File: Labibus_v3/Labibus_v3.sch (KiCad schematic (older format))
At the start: 33 parts

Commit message: update started on first pcb layout
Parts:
- added J13, J14, J15, J16, J4, J5, J6, J7: Conn_01x03, Connector_PinSocket_2.54mm:PinSocket_1x03_P2.54mm_Vertical, symbol Connector_Generic:Conn_01x03
- C1, C2, C3, C4, C5, C6, C7: renamed from C?; footprint (none) -> Capacitor_SMD:C_0603_1608Metric_Pad1.08x0.95mm_HandSolder
- D1, D2, D3: renamed from D?; footprint (none) -> LED_SMD:LED_0603_1608Metric_Pad1.05x0.95mm_HandSolder
- J1: renamed from J?; footprint (none) -> TerminalBlock_Phoenix:TerminalBlock_Phoenix_MPT-0,5-4-2.54_1x04_P2.54mm_Horizontal
- J10, J11, J12, J2, J3, J8, J9: renamed from J?; footprint (none) -> Connector_PinSocket_2.54mm:PinSocket_1x03_P2.54mm_Vertical
- R1, R2, R3, R4, R5, R6, R7, R8, R9: renamed from R?; footprint (none) -> Resistor_SMD:R_0603_1608Metric_Pad0.98x0.95mm_HandSolder
- RN1: renamed from RN?; footprint (none) -> Resistor_SMD:R_Array_Concave_4x0603
- SW1: renamed from SW?; footprint (none) -> Button_Switch_SMD:SW_SPST_EVQPE1
- U2: renamed from U?; footprint (none) -> Package_SO:SOIC-8_3.9x4.9mm_P1.27mm
- Y1: renamed from Y?; footprint (none) -> Crystal:Resonator_SMD_muRata_CSTxExxV-3Pin_3.0x1.1mm_HandSoldering
- gave numbers to parts that had none: 2
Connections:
- net D6 is gone; now on net ARDUINO_P6: U3.10 (PD6)
- net D7 is gone; now on net ARDUINO_P7: U3.11 (PD7)
- net RX is gone; now on net ARDUINO_P_RX: J3.4 (Pin_4)
- net TX is gone; now on net ARDUINO_P_TX: J3.5 (Pin_5)
- net +5V: now also J13.2 (Pin_2), J14.2 (Pin_2), J15.2 (Pin_2), J16.2 (Pin_2), J4.2 (Pin_2), J5.2 (Pin_2), J6.2 (Pin_2), J7.2 (Pin_2)
- net A6: now also J6.3 (Pin_3)
- net A7: now also J15.3 (Pin_3)
- net D2: now also J4.3 (Pin_3)
- net D3: now also J13.3 (Pin_3)
- net D4: now also J5.3 (Pin_3)
- net D5: now also J14.3 (Pin_3)
- net D8: now also J7.3 (Pin_3)
- net D9: now also J16.3 (Pin_3)
- net GND: now also J13.1 (Pin_1), J14.1 (Pin_1), J15.1 (Pin_1), J16.1 (Pin_1), J4.1 (Pin_1), J5.1 (Pin_1), J6.1 (Pin_1), J7.1 (Pin_1)
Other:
- note added: "A6-pinout"
- note added: "A7-pinout"
- note added: "D2-pinout"
- note added: "D3-pinout"
- note added: "D4-pinout"
- note added: "D5-pinout"
- note added: "D8-pinout"
- note added: "D9-pinout"
- moved on the sheet: C6, C7, U3

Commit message: new update to the pcb layout Note: Change pin row to 13 on the left side to shrink the size
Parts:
- J10: footprint Connector_PinSocket_2.54mm:PinSocket_1x03_P2.54mm_Vertical -> Connector_PinSocket_2.54mm:PinSocket_1x06_P2.54mm_Vertical
- J2: footprint Connector_PinSocket_2.54mm:PinSocket_1x03_P2.54mm_Vertical -> Connector_PinHeader_2.54mm:PinHeader_1x04_P2.54mm_Vertical
- J3: footprint Connector_PinSocket_2.54mm:PinSocket_1x03_P2.54mm_Vertical -> Connector_PinHeader_2.54mm:PinHeader_1x06_P2.54mm_Vertical
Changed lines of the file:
@@
 F 0 "J3" H 8093 1442 50  0000 C CNN
 F 1 "Conn_01x06" H 8093 1351 50  0000 C CNN
-F 2 "Connector_PinSocket_2.54mm:PinSocket_1x03_P2.54mm_Vertical" H 8175 1025 50  0001 C CNN
+F 2 "Connector_PinHeader_2.54mm:PinHeader_1x06_P2.54mm_Vertical" H 8175 1025 50  0001 C CNN
 F 3 "~" H 8175 1025 50  0001 C CNN
 	1    8175 1025
@@
 F 0 "J10" H 10605 1042 50  0000 L CNN
 F 1 "Conn_01x06" H 10605 951 50  0000 L CNN
-F 2 "Connector_PinSocket_2.54mm:PinSocket_1x03_P2.54mm_Vertical" H 10525 1050 50  0001 C CNN
+F 2 "Connector_PinSocket_2.54mm:PinSocket_1x06_P2.54mm_Vertical" H 10525 1050 50  0001 C CNN
 F 3 "~" H 10525 1050 50  0001 C CNN
 	1    10525 1050
@@
 F 0 "J2" H 8055 1792 50  0000 L CNN
 F 1 "Conn_01x04" H 8055 1701 50  0000 L CNN
-F 2 "Connector_PinSocket_2.54mm:PinSocket_1x03_P2.54mm_Vertical" H 7975 1800 50  0001 C CNN
+F 2 "Connector_PinHeader_2.54mm:PinHeader_1x04_P2.54mm_Vertical" H 7975 1800 50  0001 C CNN
 F 3 "~" H 7975 1800 50  0001 C CNN
 	1    7975 1800

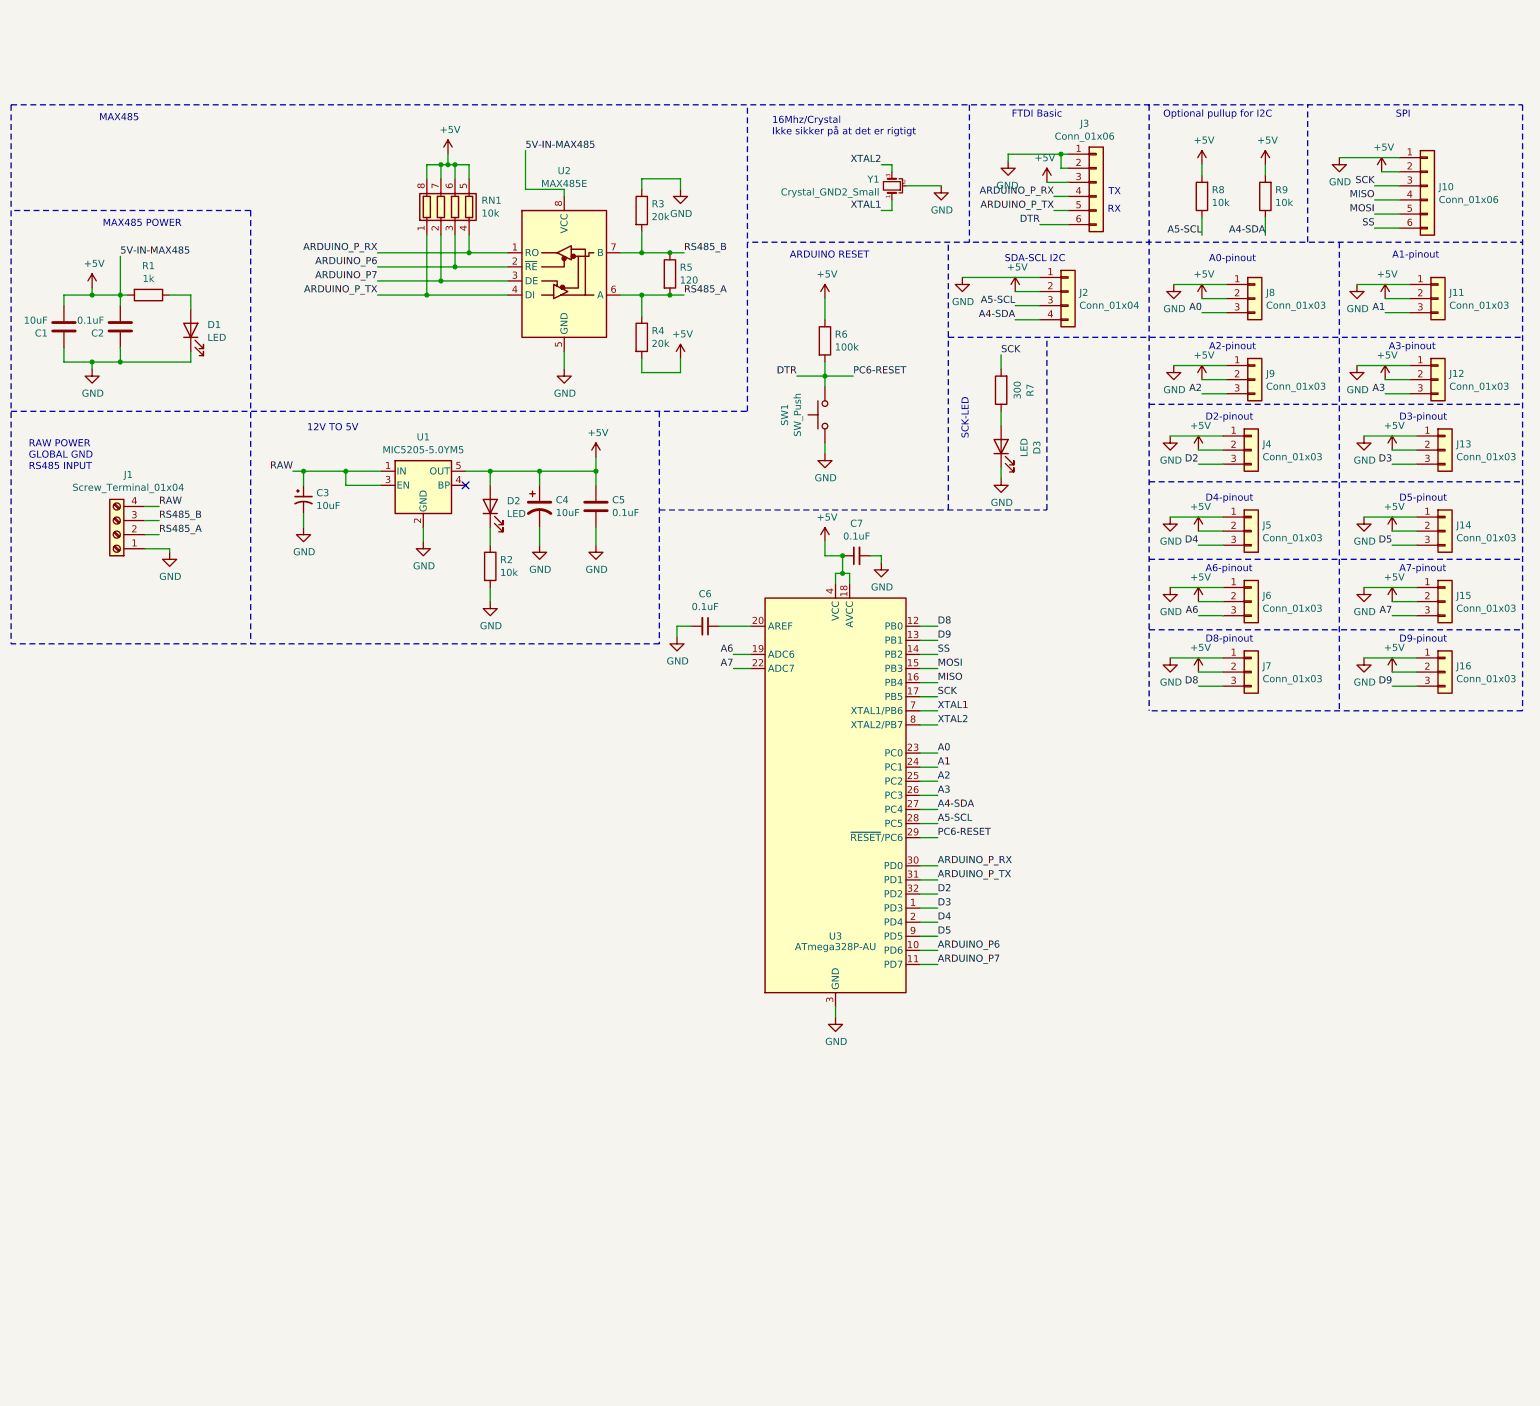
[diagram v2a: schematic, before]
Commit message: added tabel and price. board version 1.2
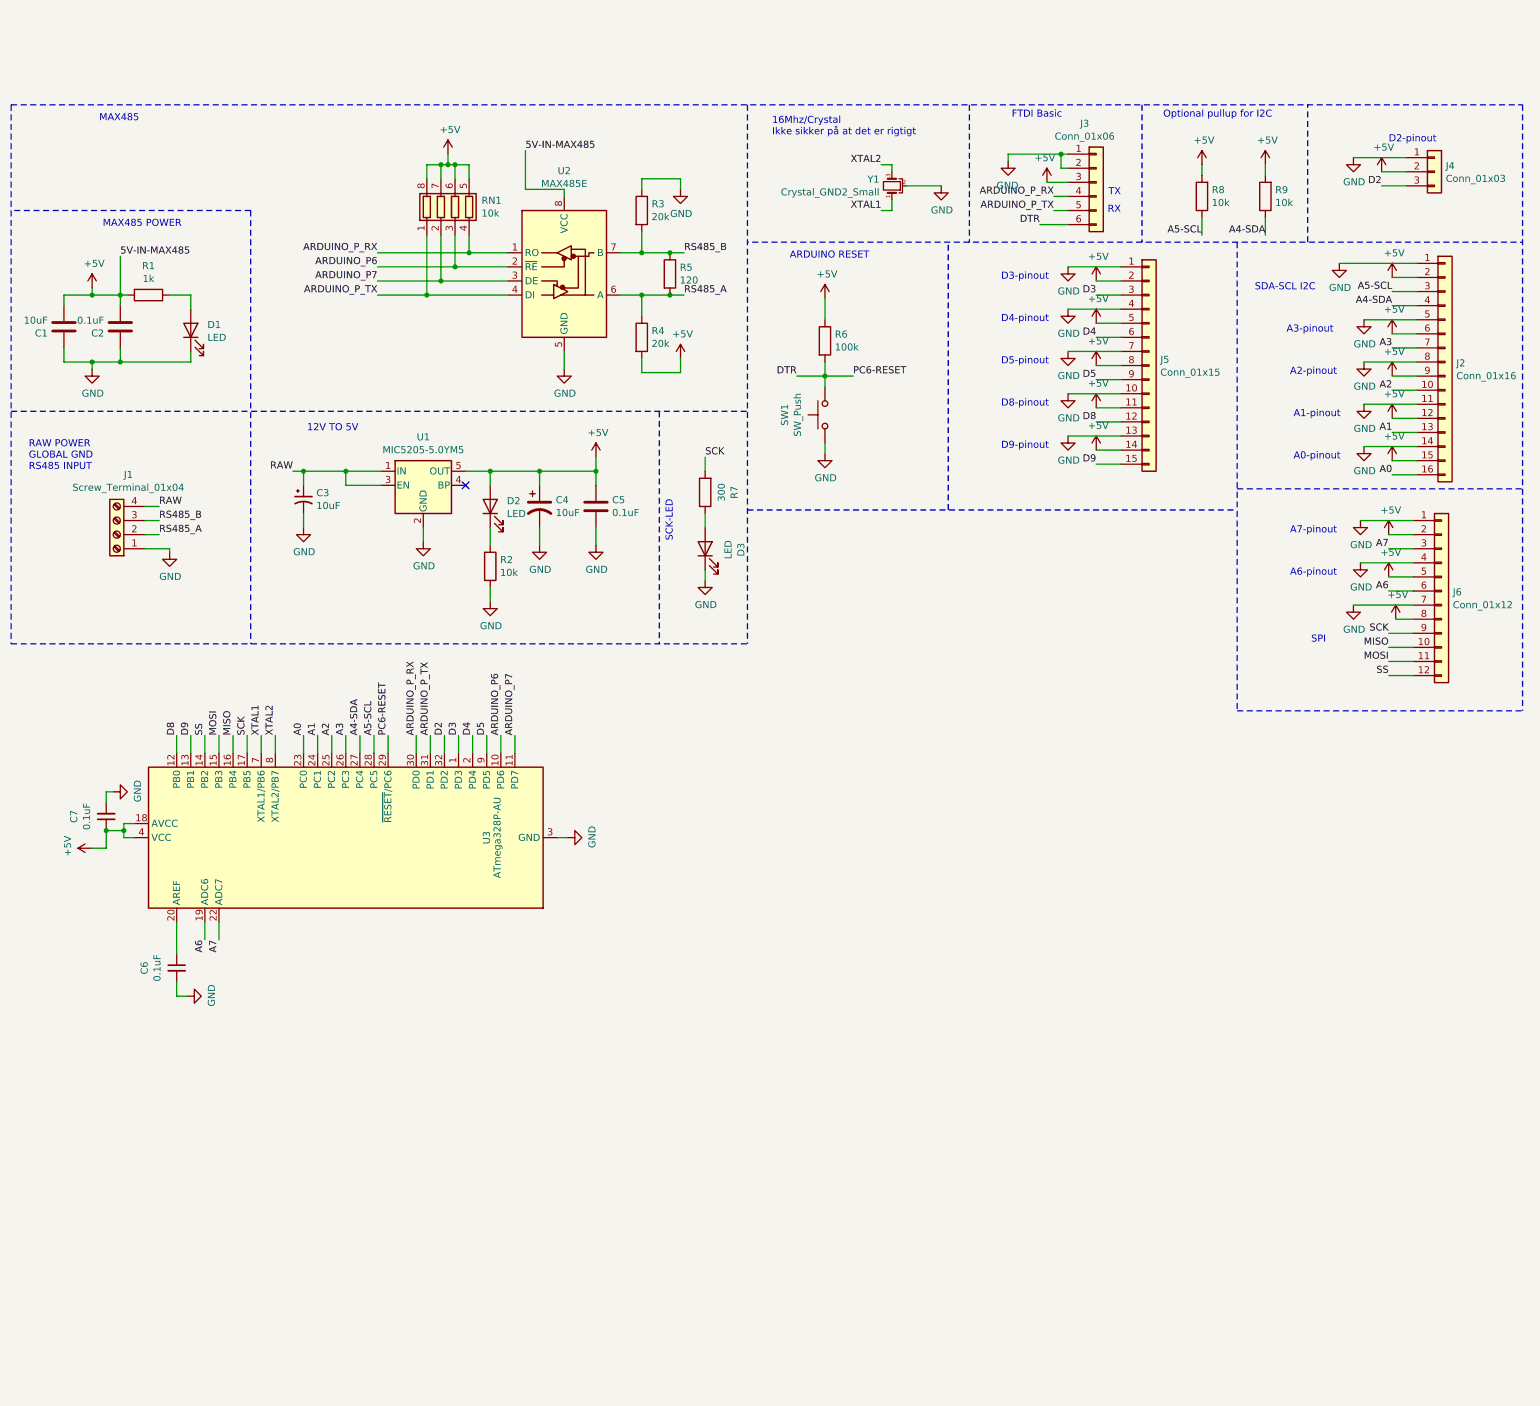
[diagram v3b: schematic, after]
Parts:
- removed J10: Conn_01x06, Connector_PinSocket_2.54mm:PinSocket_1x06_P2.54mm_Vertical, symbol Connector_Generic:Conn_01x06
- removed J11, J12, J13, J14, J15, J16, J5, J6, J7, J8, J9: Conn_01x03, Connector_PinSocket_2.54mm:PinSocket_1x03_P2.54mm_Vertical, symbol Connector_Generic:Conn_01x03
- removed J2: Conn_01x04, Connector_PinHeader_2.54mm:PinHeader_1x04_P2.54mm_Vertical, symbol Connector_Generic:Conn_01x04
- added J2: Conn_01x16, Connector_PinSocket_2.54mm:PinSocket_1x16_P2.54mm_Vertical, symbol Connector_Generic:Conn_01x16
- added J5: Conn_01x15, Connector_PinSocket_2.54mm:PinSocket_1x15_P2.54mm_Vertical, symbol Connector_Generic:Conn_01x15
- added J6: Conn_01x12, Connector_PinSocket_2.54mm:PinSocket_1x12_P2.54mm_Vertical, symbol Connector_Generic:Conn_01x12
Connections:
- net +5V: now also J2.12 (Pin_12), J2.15 (Pin_15), J2.2 (Pin_2), J2.6 (Pin_6), J2.9 (Pin_9), J5.11 (Pin_11), J5.14 (Pin_14), J5.2 (Pin_2), J5.5 (Pin_5), J5.8 (Pin_8), J6.2 (Pin_2), J6.5 (Pin_5), J6.8 (Pin_8)
- net A0: now also J2.16 (Pin_16)
- net A1: now also J2.13 (Pin_13)
- net A2: now also J2.10 (Pin_10)
- net A3: now also J2.7 (Pin_7)
- net A4-SDA: now also J2.4 (Pin_4)
- net A5-SCL: now also J2.3 (Pin_3)
- net A6: now also J6.6 (Pin_6)
- net A7: now also J6.3 (Pin_3)
- net D3: now also J5.3 (Pin_3)
- net D4: now also J5.6 (Pin_6)
- net D5: now also J5.9 (Pin_9)
- net D8: now also J5.12 (Pin_12)
- net D9: now also J5.15 (Pin_15)
- net GND: now also J2.1 (Pin_1), J2.11 (Pin_11), J2.14 (Pin_14), J2.5 (Pin_5), J2.8 (Pin_8), J5.1 (Pin_1), J5.10 (Pin_10), J5.13 (Pin_13), J5.4 (Pin_4), J5.7 (Pin_7), J6.1 (Pin_1), J6.4 (Pin_4), J6.7 (Pin_7)
- net MISO: now also J6.10 (Pin_10)
- net MOSI: now also J6.11 (Pin_11)
- net SCK: now also J6.9 (Pin_9)
- net SS: now also J6.12 (Pin_12)
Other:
- moved on the sheet: C6, C7, D3, J4, R7, U3

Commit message: update to the pcb. 3v3 added I2C 3.3 and 5 JST added.
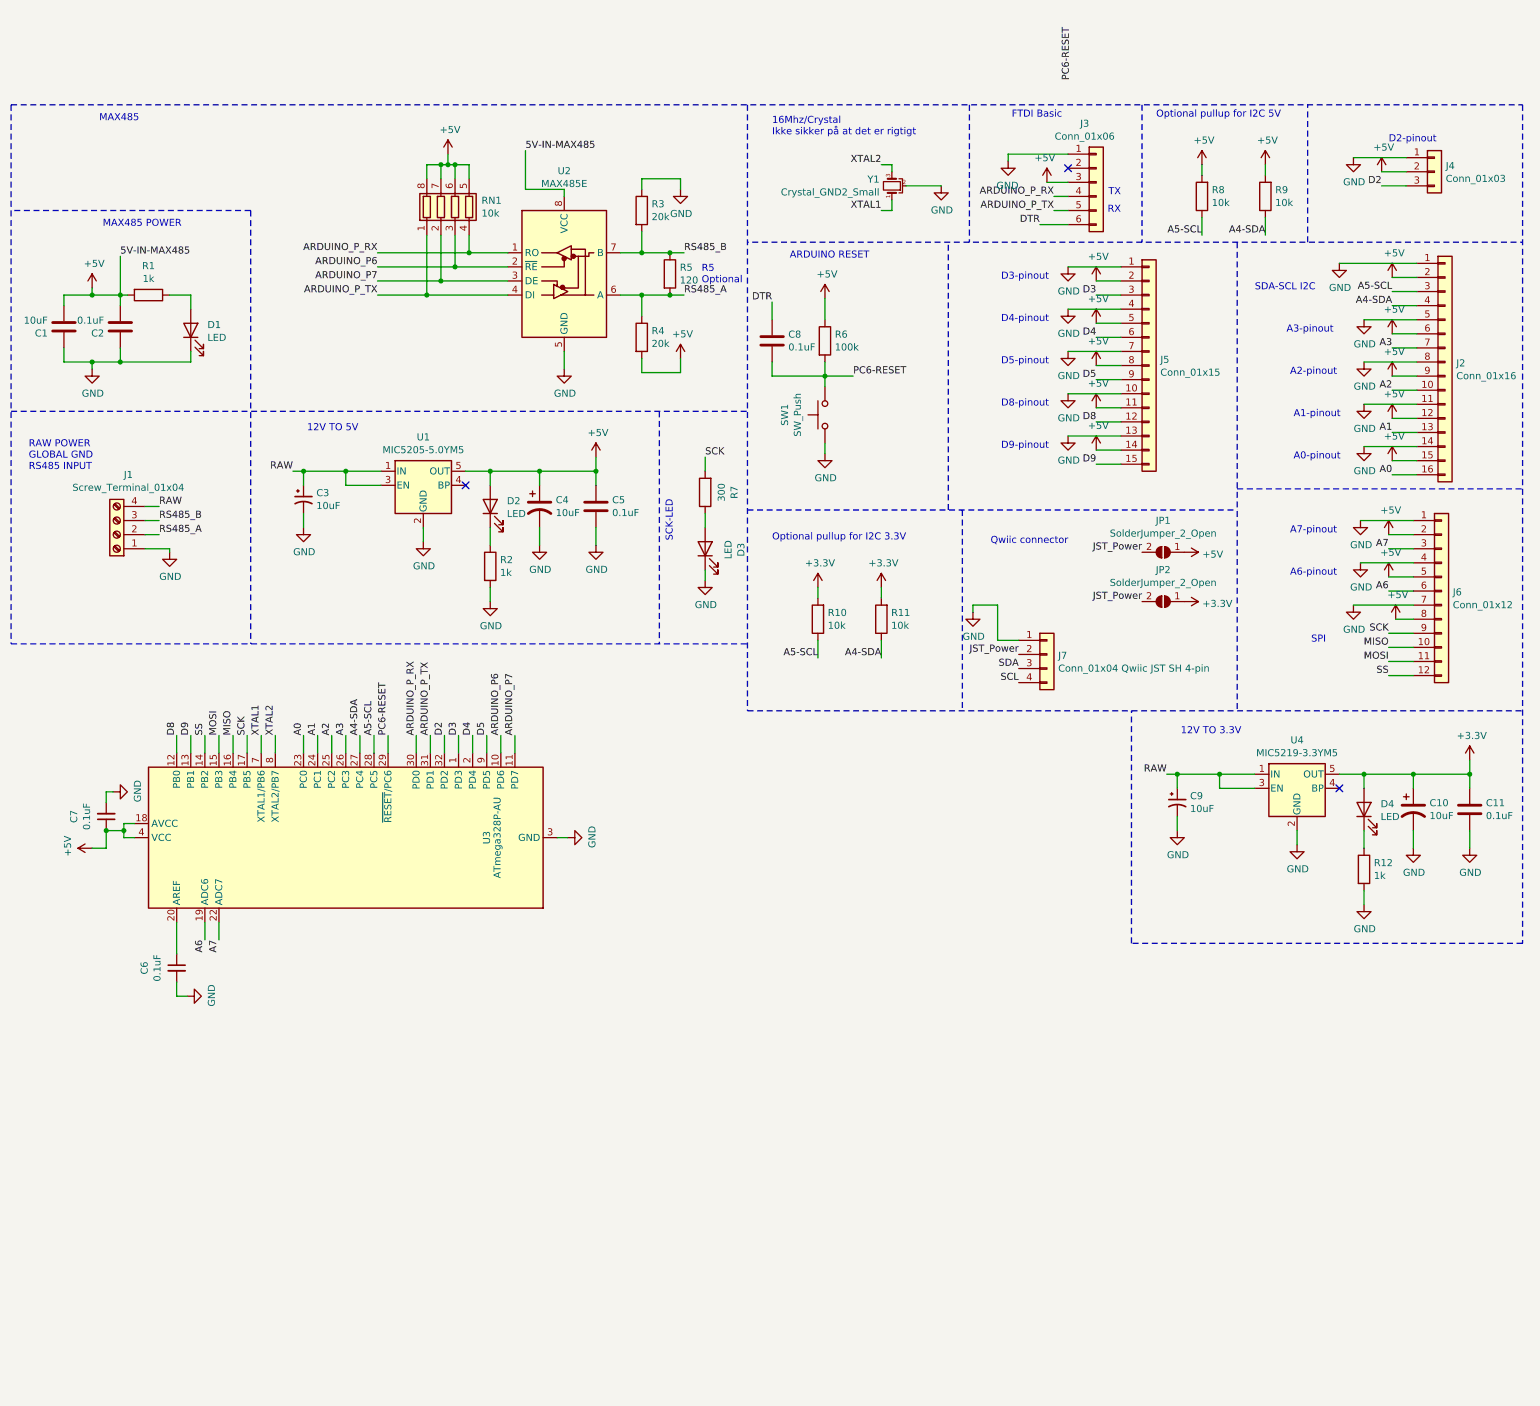
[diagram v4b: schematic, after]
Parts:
- added C10: 10uF, Capacitor_SMD:C_0603_1608Metric_Pad1.08x0.95mm_HandSolder, symbol Device:CP1
- added C11, C8: 0.1uF, Capacitor_SMD:C_0603_1608Metric_Pad1.08x0.95mm_HandSolder, symbol Device:C
- added C9: 10uF, Capacitor_SMD:C_0603_1608Metric_Pad1.08x0.95mm_HandSolder, symbol Device:CP1_Small
- added D4: LED, LED_SMD:LED_0603_1608Metric_Pad1.05x0.95mm_HandSolder, symbol Device:LED
- added J7: Conn_01x04 Qwiic JST SH 4-pin, Connector_PinSocket_1.00mm:PinSocket_1x04_P1.00mm_Vertical_SMD_Pin1Left, symbol Connector_Generic:Conn_01x04
- added JP1, JP2: SolderJumper_2_Open, Jumper:SolderJumper-2_P1.3mm_Open_RoundedPad1.0x1.5mm, symbol Jumper:SolderJumper_2_Open
- added R10, R11: 10k, Resistor_SMD:R_0603_1608Metric_Pad0.98x0.95mm_HandSolder, symbol Device:R
- added R12: 1k, Resistor_SMD:R_0603_1608Metric_Pad0.98x0.95mm_HandSolder, symbol Device:R
- added U4: MIC5219-3.3YM5, Package_TO_SOT_SMD:SOT-23-5, symbol Regulator_Linear:MIC5219-3.3YM5
- R2: value 10k -> 1k
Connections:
- net +5V: now also JP1.1 (A)
- net A4-SDA: now also R11.1
- net A5-SCL: now also R10.1
- net DTR: now also C8.2; no longer R6.2, SW1.2, U3.29 (~RESET~/PC6)
- net GND: now also C10.2, C11.2, C9.2, J7.1 (Pin_1), R12.2, U4.2 (GND); no longer J3.2 (Pin_2)
- net RAW: now also C9.1, U4.1 (IN), U4.3 (EN)
- new net: D4.1 (K), R12.1
- new net +3V3: C10.1, C11.1, D4.2 (A), JP2.1 (A), R10.2, R11.2, U4.5 (OUT)
- new net JST_Power: J7.2 (Pin_2), JP1.2 (B), JP2.2 (B)
- new net PC6-RESET: C8.1, R6.2, SW1.2, U3.29 (~RESET~/PC6)
- new net SCL: J7.4 (Pin_4)
- new net SDA: J7.3 (Pin_3)
- no-connect marks 1 -> 3
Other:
- note added: "12V TO 3.3V"
- note added: "Optional pullup for I2C 3.3V"
- note added: "Optional pullup for I2C 5V"
- note added: "Qwiic connector"
- note added: "R5\nOptional"
- note removed: "Optional pullup for I2C"
